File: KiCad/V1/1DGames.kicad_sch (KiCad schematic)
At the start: 17 parts, among them Q1 AO3401A, Q2 AO3401A, U1 ESP32-DEVKITC-32D

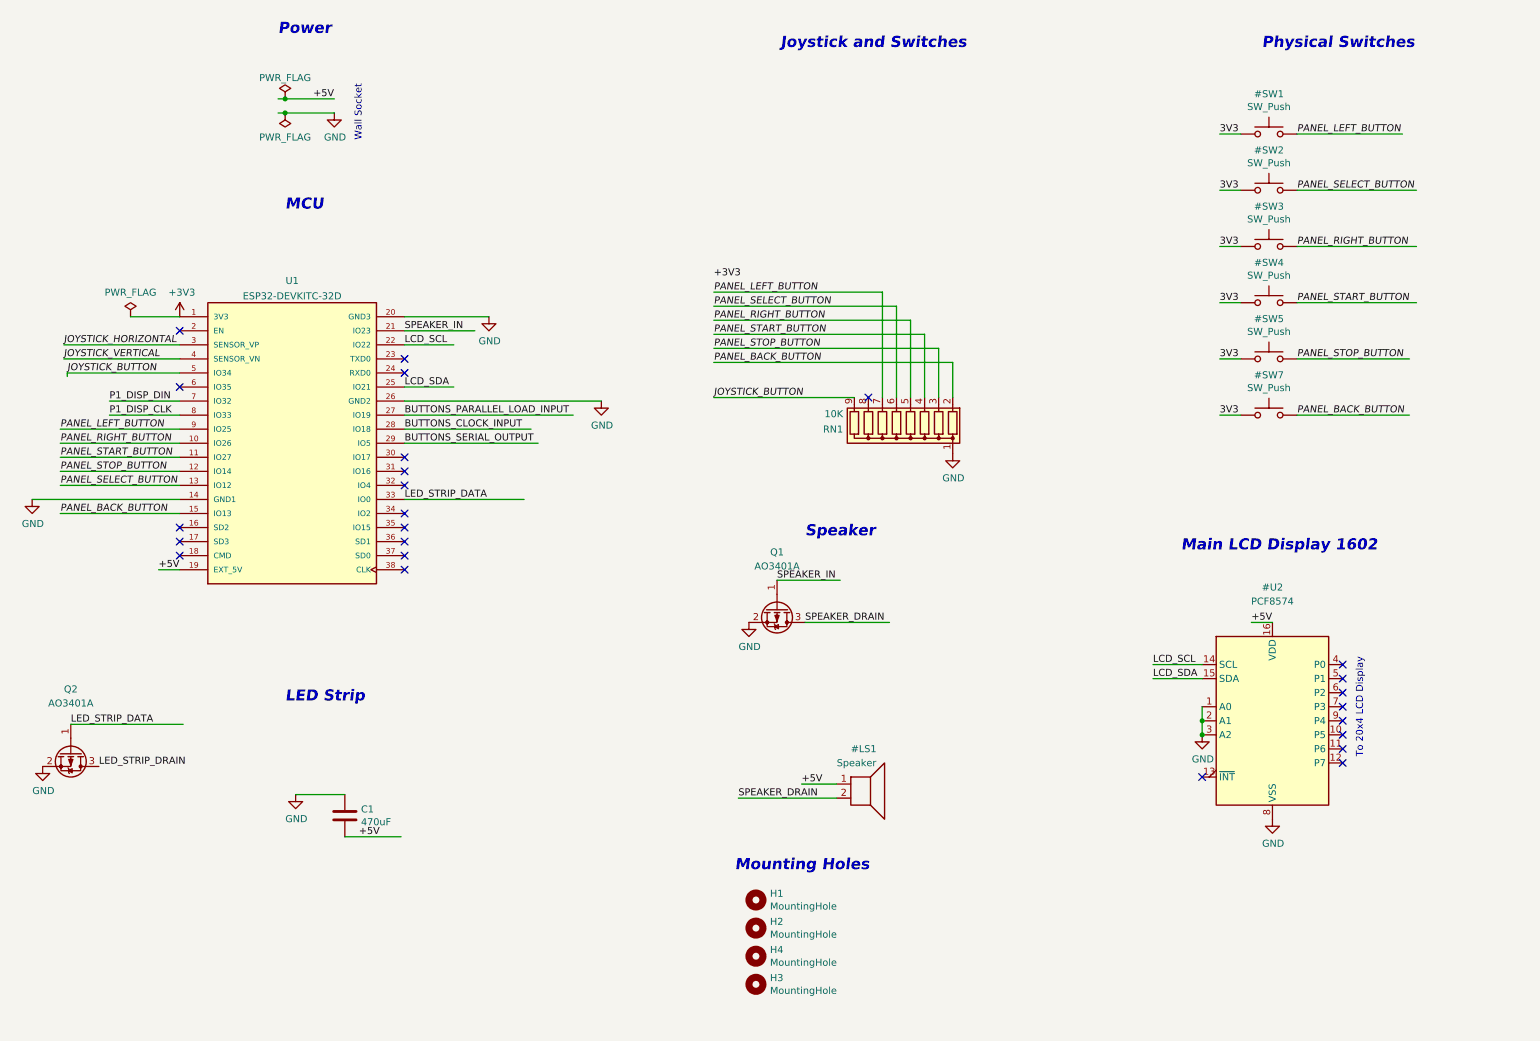
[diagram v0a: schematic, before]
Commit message: Worms joystick working, next: show joystick status in UI (including button).
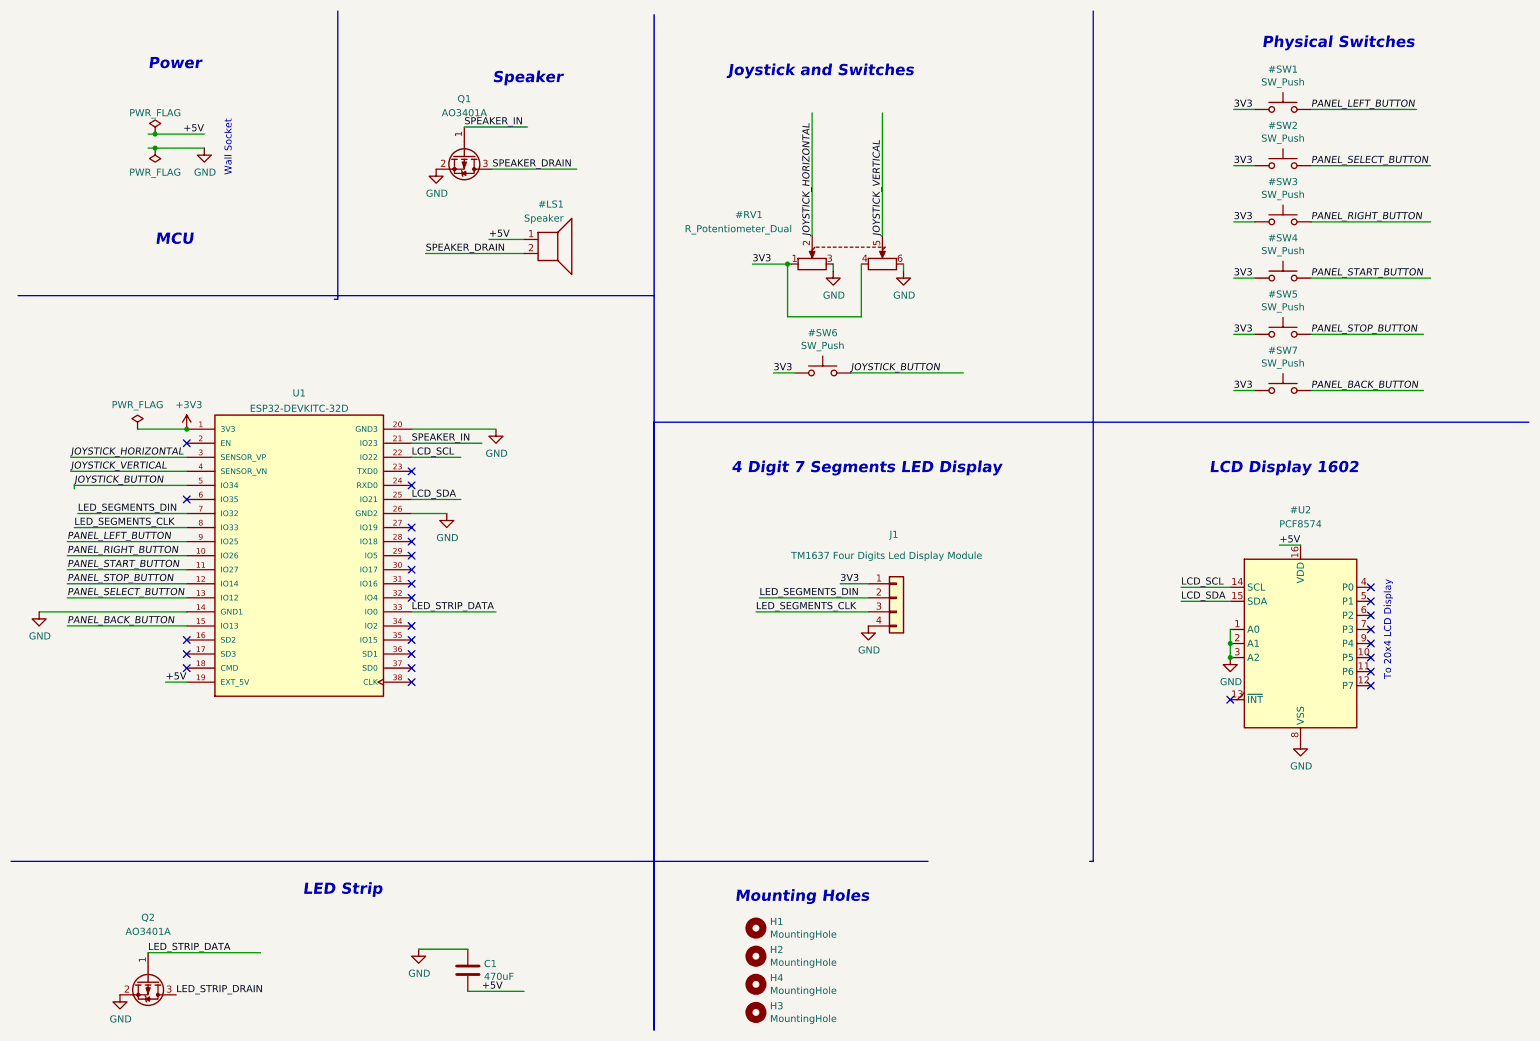
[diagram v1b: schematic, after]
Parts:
- removed RN1: 10K, Resistor_THT:R_Array_SIP9, symbol Device:R_Network08
- added #RV1: R_Potentiometer_Dual, symbol Device:R_Potentiometer_Dual
- added #SW6: SW_Push, symbol Switch:SW_Push
- added J1: TM1637 Four Digits Led Display Module, symbol Connector_Generic:Conn_01x04
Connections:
- net 3V3: now also #RV1.1, #RV1.4, #SW6.1, J1.1 (Pin_1)
- net GND: now also #RV1.3, #RV1.6, J1.4 (Pin_4)
- net JOYSTICK_BUTTON: now also #SW6.2
- net JOYSTICK_HORIZONTAL: now also #RV1.2
- net JOYSTICK_VERTICAL: now also #RV1.5
- net BUTTONS_CLOCK_INPUT: no longer names the net of U1.28 (IO18)
- net BUTTONS_PARALLEL_LOAD_INPUT: no longer names the net of U1.27 (IO19)
- net BUTTONS_SERIAL_OUTPUT: no longer names the net of U1.29 (IO5)
- net P1_DISP_CLK renamed LED_SEGMENTS_CLK
- net LED_SEGMENTS_CLK: now also J1.3 (Pin_3)
- net P1_DISP_DIN renamed LED_SEGMENTS_DIN
- net LED_SEGMENTS_DIN: now also J1.2 (Pin_2)
- no-connect marks 25 -> 27
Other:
- note added: "4 Digit 7 Segments LED Display"
- note added: "LCD Display 1602"
- note removed: "Main LCD Display 1602"
- moved on the sheet: C1, H1, H2, H3, H4, Q1, Q2, U1
